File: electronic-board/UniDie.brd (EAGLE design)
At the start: 100 x 80 mm, 23 parts, among them IC1 ATMEGA88-THIN, J1 PJ-037A, J2 AVR_SPI_PROG_3X2NS

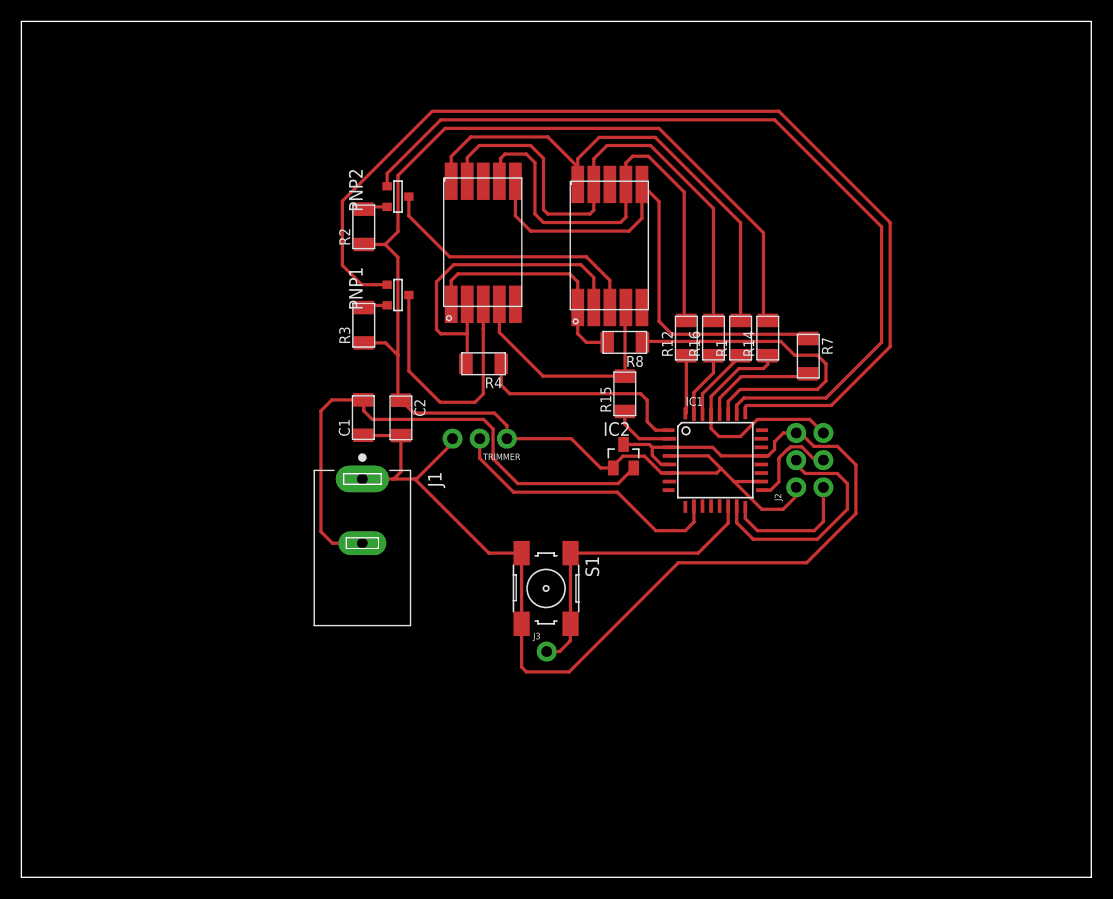
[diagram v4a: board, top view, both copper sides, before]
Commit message: Updated dxf layout on board. Removed dc plug and added power pins. Added holes to board
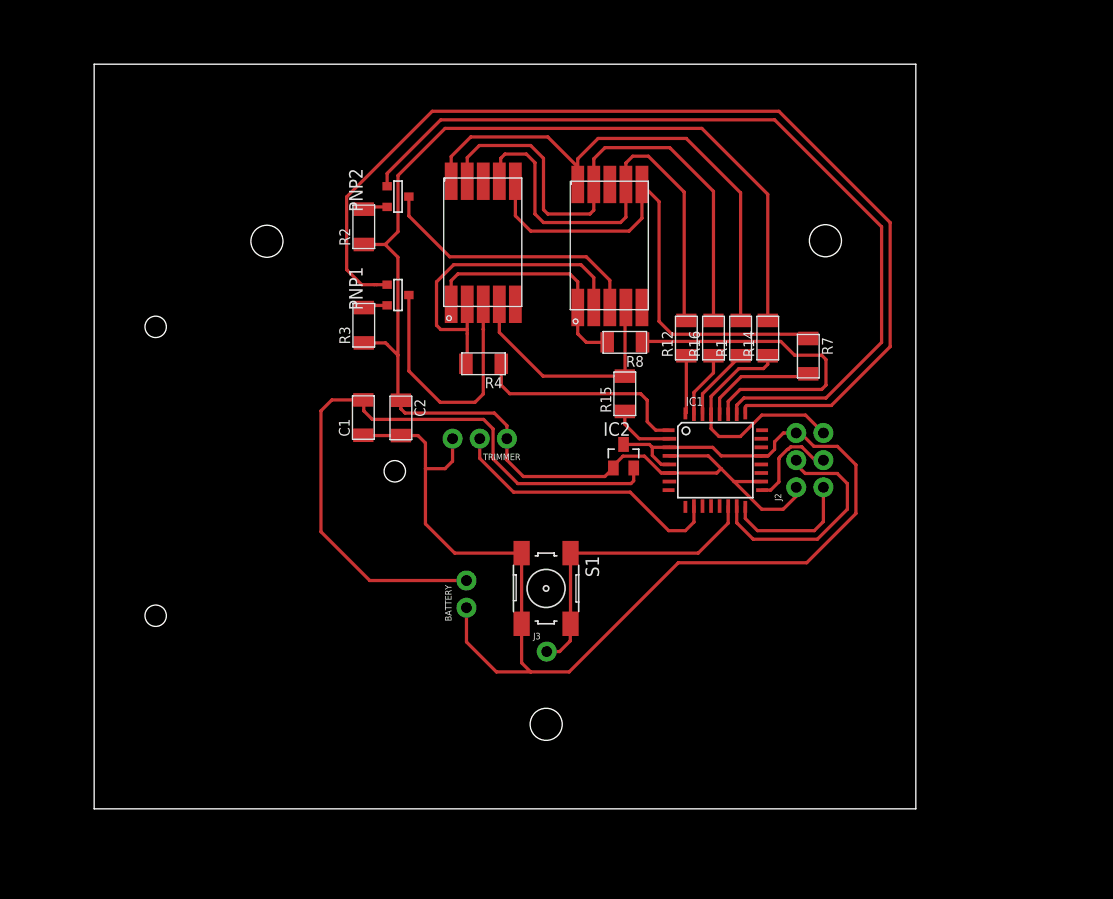
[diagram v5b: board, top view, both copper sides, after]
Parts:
- removed J1: PJ-037A, PJ-037A:CUI_PJ-037A
- added BATTERY: (no value), SparkFun-Connectors:1X02_NO_SILK
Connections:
- net GND: now also BATTERY.1; no longer J1.1
- net N$1: now also BATTERY.2; no longer J1.2
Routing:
- net N$1: track 51.3 -> 63.2 mm
- net GND: track 111.1 -> 119.0 mm
- net 5V: track 128.6 -> 133.3 mm
- net SEG10: track 48.6 -> 50.1 mm
- net SEG9: track 49.5 -> 50.3 mm
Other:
- board size 100 x 80 mm -> 76.8 x 69.6 mm

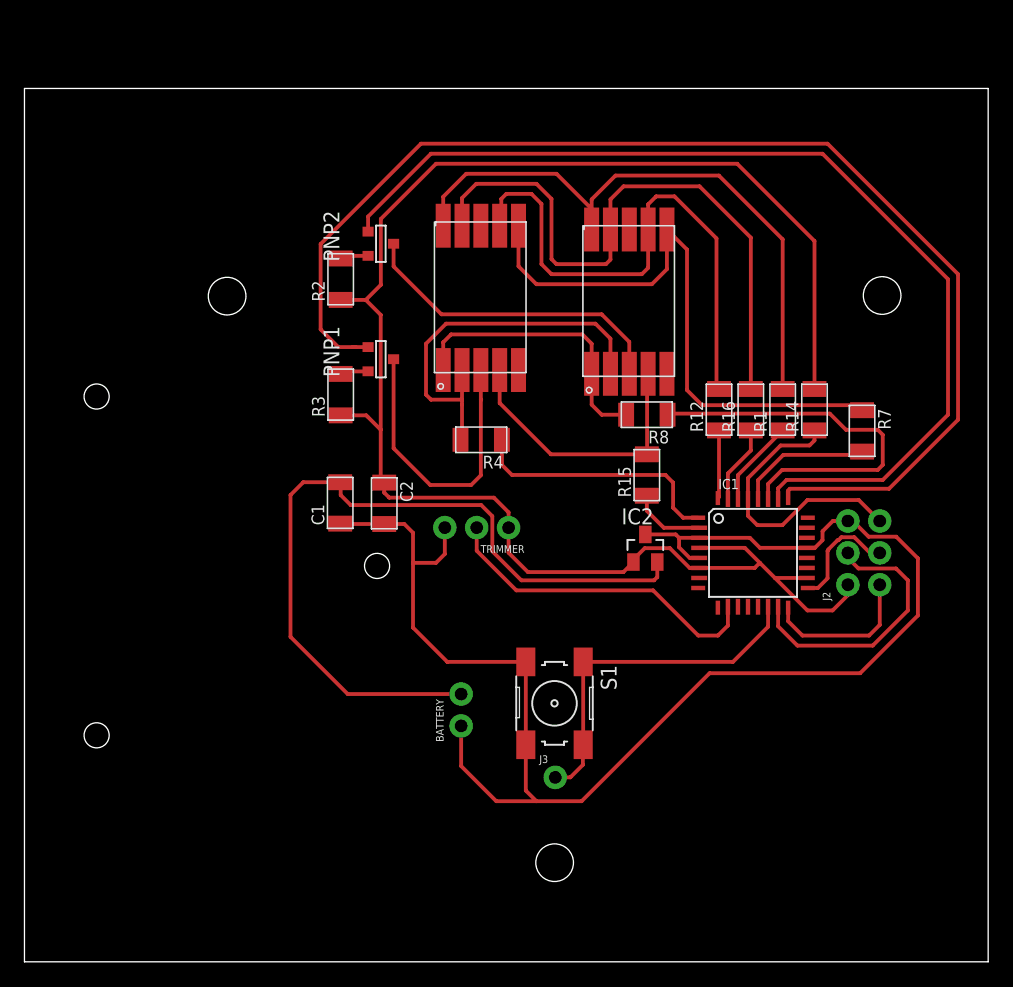
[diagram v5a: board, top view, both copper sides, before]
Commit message: Updated board design with potentiomenter layout and traces optimizations
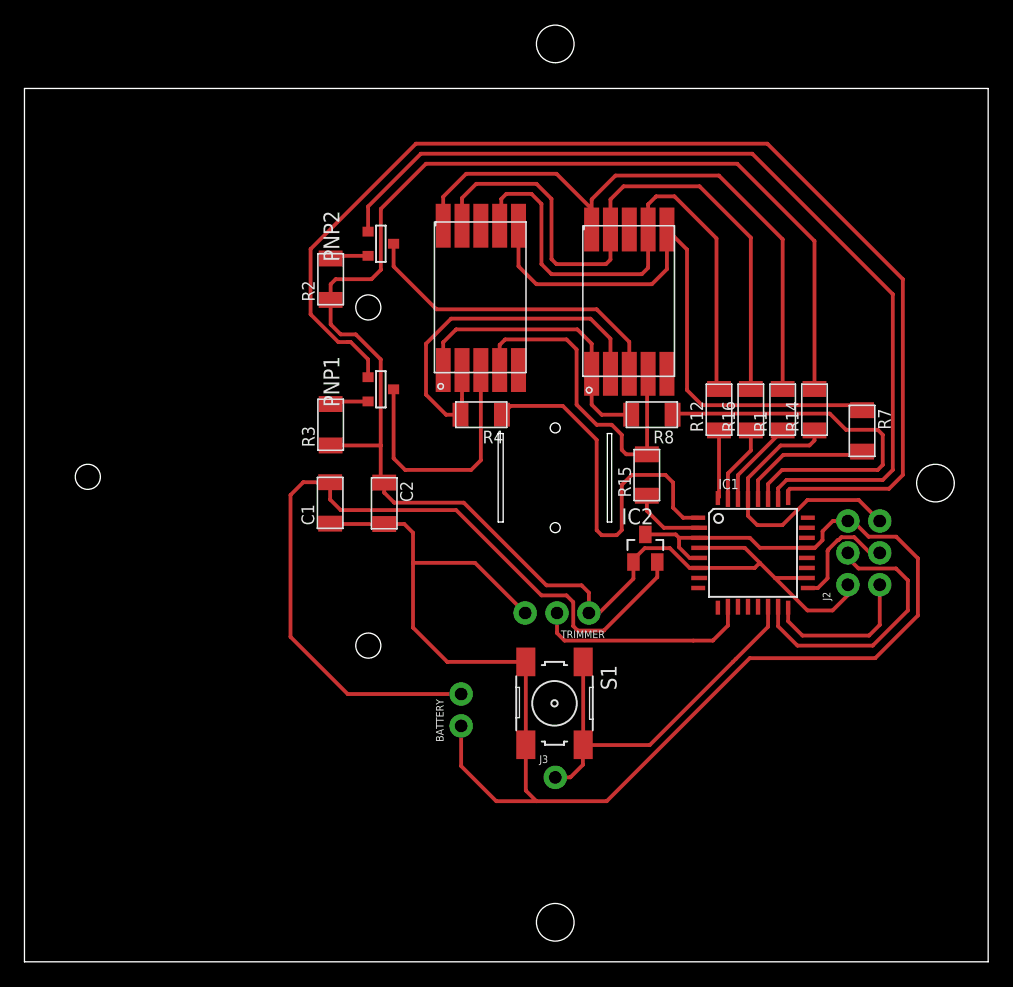
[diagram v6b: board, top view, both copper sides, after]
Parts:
- moved TRIMMER 9.34 mm to (51.8, 34.2)
- moved R3 2.53 mm to (31.2, 49.2)
- moved PNP1 2.40 mm to (35.2, 52.0)
- moved R4 2.00 mm to (43.2, 50.0)
- moved C1 0.80 mm to (31.2, 43.0)
- moved R2 0.80 mm to (31.2, 60.8)
- moved R8 0.40 mm to (56.8, 50.0)
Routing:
- net N$7: track 20.6 -> 31.1 mm
- net TRM: track 26.5 -> 17.5 mm
- net 5V: track 133.3 -> 139.8 mm
- net GND: track 119.0 -> 125.5 mm
- net GT1: track 81.2 -> 74.8 mm
- net SEG4: track 22.5 -> 27.4 mm
- net GT2: track 97.7 -> 93.7 mm
- net DIG2: track 24.0 -> 20.3 mm
- net N$1: track 63.2 -> 66.2 mm
- net SWT: track 28.3 -> 31.1 mm
- net N$2: track 2.27 -> 3.07 mm
- net N$13: track 2.39 -> 3.19 mm
- net SEG1: track 22.5 -> 23.3 mm
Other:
- outline, holes or cut-outs redrawn

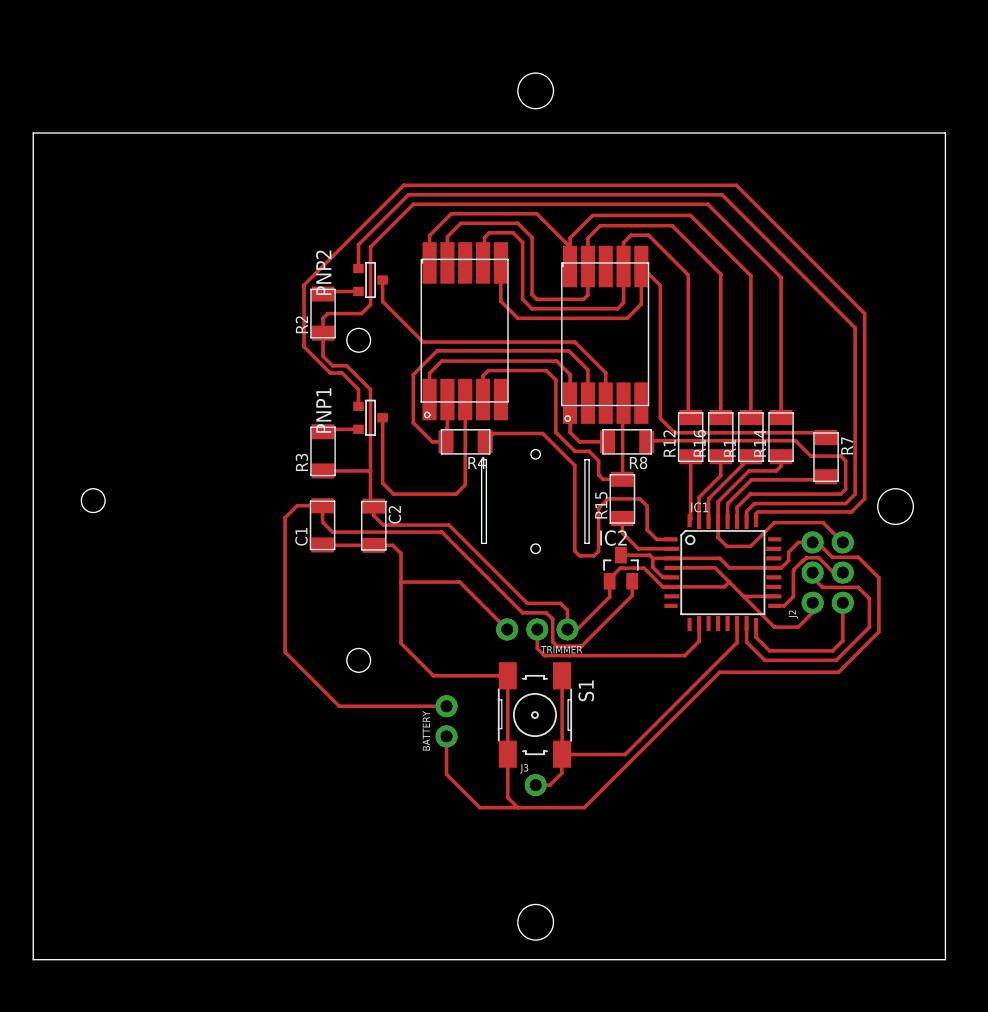
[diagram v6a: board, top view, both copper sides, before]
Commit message: Added circuit breaker to board to switch on/off power
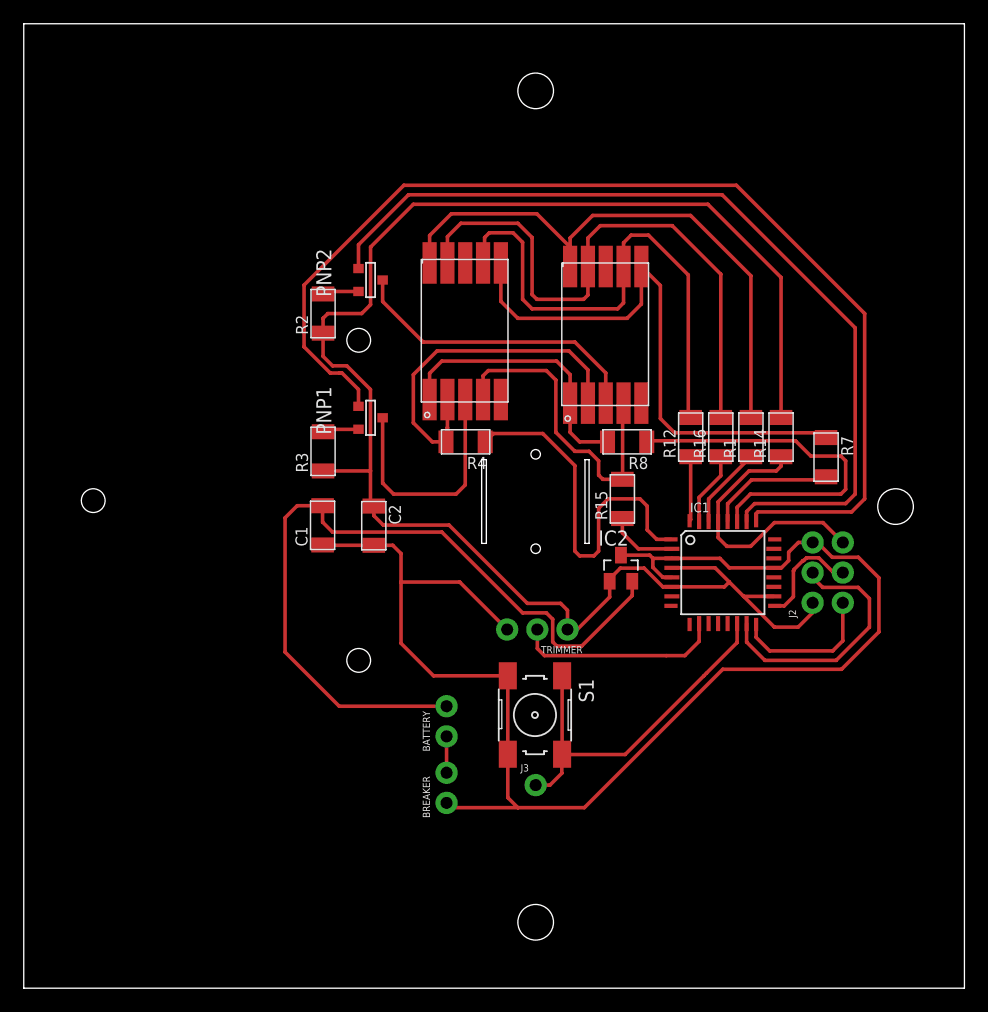
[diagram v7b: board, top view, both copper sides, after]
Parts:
- added BREAKER: (no value), SparkFun-Connectors:1X02_NO_SILK
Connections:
- new net N$5: BATTERY.1, BREAKER.2
- net GND: now also BREAKER.1; no longer BATTERY.1
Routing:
- net GND: track 125.5 -> 121.3 mm
- net N$5: track 0.00 -> 3.06 mm
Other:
- board size 76.8 x 69.6 mm -> 79.2 x 81.2 mm
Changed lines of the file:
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@@
 <board>
 <plain>
-<wire x1="6.8" y1="6.4" x2="83.6" y2="6.4" width="0" layer="20"/>
-<wire x1="83.6" y1="6.4" x2="83.6" y2="76" width="0" layer="20"/>
-<wire x1="83.6" y1="76" x2="6.8" y2="76" width="0" layer="20"/>
-<wire x1="6.8" y1="76" x2="6.8" y2="6.4" width="0" layer="20"/>
+<wire x1="6" y1="4" x2="85.2" y2="4" width="0" layer="20"/>
+<wire x1="85.2" y1="4" x2="85.2" y2="85.2" width="0" layer="20"/>
+<wire x1="85.2" y1="85.2" x2="6" y2="85.2" width="0" layer="20"/>
+<wire x1="6" y1="85.2" x2="6" y2="4" width="0" layer="20"/>
 <hole x="49.1" y="79.55" drill="3"/>
 <hole x="79.4" y="44.55" drill="3"/>
@@
 <element name="J3" library="SparkFun-Connectors" package="1X01_NO_SILK" value="" x="49.1" y="21.1"/>
 <element name="BATTERY" library="SparkFun-Connectors" package="1X02_NO_SILK" value="" x="41.6" y="25.2" rot="R90"/>
+<element name="BREAKER" library="SparkFun-Connectors" package="1X02_NO_SILK" value="" x="41.6" y="19.6" rot="R90"/>
 </elements>
 <signals>
 <signal name="GND">
-<contactref element="C1" pad="1"/>
-<contactref element="IC2" pad="3"/>
 <contactref element="C2" pad="2"/>
 <contactref element="IC1" pad="21"/>
@@
 <contactref element="S1" pad="4"/>
 <contactref element="S1" pad="3"/>
-<wire x1="64.6" y1="30.6" x2="53.2" y2="19.2" width="0.3048" layer="1"/>
+<wire x1="64.85" y1="30.85" x2="53.2" y2="19.2" width="0.3048" layer="1"/>
 <wire x1="46.754" y1="23.698" x2="46.754" y2="30.302" width="0.3048" layer="1"/>
 <wire x1="46.754" y1="23.698" x2="46.754" y2="20.046" width="0.3048" layer="1"/>
@@
 <wire x1="47.6" y1="19.2" x2="53.2" y2="19.2" width="0.3048" layer="1"/>
 <wire x1="78" y1="38.55" x2="78" y2="34" width="0.3048" layer="1"/>
-<wire x1="78" y1="34" x2="74.6" y2="30.6" width="0.3048" layer="1"/>
-<wire x1="74.6" y1="30.6" x2="64.6" y2="30.6" width="0.3048" layer="1"/>
-<wire x1="31.16" y1="41.319" x2="31.19" y2="41.289" width="0.3048" layer="1"/>
-<wire x1="31.19" y1="41.289" x2="35.47" y2="41.289" width="0.3048" layer="1"/>
+<wire x1="78" y1="34" x2="74.85" y2="30.85" width="0.3048" layer="1"/>
+<wire x1="74.85" y1="30.85" x2="64.85" y2="30.85" width="0.3048" layer="1"/>
 <wire x1="60.5674" y1="40.19" x2="64.61" y2="40.19" width="0.3048" layer="1"/>
 <wire x1="64.61" y1="40.19" x2="65.41" y2="39.39" width="0.3048" layer="1"/>
 <wire x1="69.1526" y1="39.39" x2="65.41" y2="39.39" width="0.3048" layer="1"/>
 <wire x1="60.5674" y1="38.59" x2="59.81" y2="38.59" width="0.3048" layer="1"/>
-<wire x1="58.6974" y1="40.46" x2="56.2809" y2="40.46" width="0.3048" layer="1"/>
 <wire x1="60.5674" y1="40.19" x2="58.9674" y2="40.19" width="0.3048" layer="1"/>
 <wire x1="58.9674" y1="40.19" x2="58.6974" y2="40.46" width="0.3048" layer="1"/>
@@
 <wire x1="40.498" y1="30.302" x2="46.754" y2="30.302" width="0.3048" layer="1"/>
 <wire x1="37.07" y1="41.289" x2="35.47" y2="41.289" width="0.3048" layer="1"/>
-<contactref element="BATTERY" pad="1"/>
-<wire x1="41.6" y1="25.2" x2="41.6" y2="22" width="0.3048" layer="1"/>
-<wire x1="44.4" y1="19.2" x2="47.6" y2="19.2" width="0.3048" layer="1"/>
-<wire x1="41.6" y1="22" x2="44.4" y2="19.2" width="0.3048" layer="1"/>
 <wire x1="42.7055" y1="38.1945" x2="46.7" y2="34.2" width="0.3048" layer="1"/>
+<contactref element="IC2" pad="3"/>
+<contactref element="C1" pad="1"/>
+<contactref element="BREAKER" pad="1"/>
+<wire x1="42" y1="19.2" x2="41.6" y2="19.6" width="0.3048" layer="1"/>
+<wire x1="47.6" y1="19.2" x2="42" y2="19.2" width="0.3048" layer="1"/>
+<wire x1="58.6974" y1="40.46" x2="56.2809" y2="40.46" width="0.3048" layer="1"/>
+<wire x1="35.47" y1="41.289" x2="31.19" y2="41.289" width="0.3048" layer="1"/>
+<wire x1="31.19" y1="41.289" x2="31.16" y2="41.319" width="0.3048" layer="1"/>
 </signal>
 <signal name="N$1">
@@
 <wire x1="31.2" y1="47.549" x2="35.191" y2="47.549" width="0.3048" layer="1"/>
 <wire x1="35.47" y1="44.591" x2="35.47" y2="43.791" width="0.3048" layer="1"/>
-<wire x1="31.549" y1="58.8" x2="31.2" y2="59.149" width="0.3048" layer="1"/>
 <wire x1="35.191" y1="47.549" x2="35.191" y2="44.87" width="0.3048" layer="1"/>
-<wire x1="31.2" y1="59.149" x2="31.2" y2="57.2" width="0.3048" layer="1"/>
-<wire x1="31.2" y1="57.2" x2="32" y2="56.4" width="0.3048" layer="1"/>
+<wire x1="32" y1="56.4" x2="31.2" y2="57.2" width="0.3048" layer="1"/>
 <wire x1="32" y1="56.4" x2="33.2" y2="56.4" width="0.3048" layer="1"/>
-<wire x1="31.2" y1="59.149" x2="31.2" y2="60.4" width="0.3048" layer="1"/>
 <wire x1="34.451" y1="60.8" x2="35.2" y2="61.549" width="0.3048" layer="1"/>
-<wire x1="31.2" y1="60.4" x2="31.6" y2="60.8" width="0.3048" layer="1"/>
+<wire x1="31.6" y1="60.8" x2="31.2" y2="60.4" width="0.3048" layer="1"/>
 <wire x1="31.6" y1="60.8" x2="34.451" y2="60.8" width="0.3048" layer="1"/>
 <wire x1="55.3309" y1="38.26" x2="55.3309" y2="36.9309" width="0.3048" layer="1"/>
@@
 <wire x1="33.2" y1="56.4" x2="35.191" y2="54.409" width="0.3048" layer="1"/>
 <wire x1="35.191" y1="54.409" x2="35.191" y2="47.549" width="0.3048" layer="1"/>
+<wire x1="31.2" y1="60.4" x2="31.2" y2="59.149" width="0.3048" layer="1"/>
+<wire x1="31.2" y1="57.2" x2="31.2" y2="59.149" width="0.3048" layer="1"/>
 </signal>
 <signal name="MISO">
@@
 <wire x1="66.06" y1="44.4826" x2="66.06" y2="43.2826" width="0.3048" layer="1"/>
 </signal>
+<signal name="N$5">
+<contactref element="BREAKER" pad="2"/>
+<contactref element="BATTERY" pad="1"/>
+<wire x1="41.6" y1="22.14" x2="41.6" y2="25.2" width="0.3048" layer="1"/>
+</signal>
 </signals>
